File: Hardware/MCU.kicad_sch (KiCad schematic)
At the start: 18 parts, among them SW1 SW_Push, SW2 SW_SPDT, U1 STM32F405RGTx, Y1 Crystal

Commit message: Edited schematics
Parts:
- added C15: 100nF, symbol Device:C
- added J3: Conn_01x04_Pin, symbol Connector:Conn_01x04_Pin
- added R4, R5: 0, symbol Device:R
- added R6, R7: 10k, symbol Device:R
- C11: value 10uF -> 100nF
- C12, C13: value C -> 2.2uF
- R1: value R -> 10k
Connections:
- net +3.3V: now also J3.1 (Pin_1), R4.2, R5.2
- net GND: now also C15.2, J3.2 (Pin_2), R6.2
- net Baro_SCK: now reaches U1.21 (PA5)
- net Baro_MISO: now reaches U1.22 (PA6)
- net Baro_MOSI: now reaches U1.23 (PA7)
- net Baro_SS: now reaches U1.24 (PC4)
- net V_sense: now reaches U1.27 (PB1)
- net V_sense: now also C15.1, R6.1, R7.2
- net Buzz: now reaches U1.29 (PB10)
- net ADXL_SS: now reaches U1.33 (PB12)
- net Acc_Gyro_CLK: now reaches U1.34 (PB13)
- net Acc_Gyro_MISO: now reaches U1.35 (PB14)
- net Acc_Gyro_MOSI: now reaches U1.36 (PB15)
- net ICM_SS: now reaches U1.37 (PC6)
- net SDIO_D0: now reaches U1.39 (PC8)
- net SDIO_D1: now reaches U1.40 (PC9)
- net Relay1: now reaches U1.41 (PA8)
- net Relay2: now reaches U1.42 (PA9)
- net Relay3: now reaches U1.43 (PA10)
- net USB_D-: now reaches U1.44 (PA11)
- net USB_D+: now reaches U1.45 (PA12)
- net SWDIO: now reaches U1.46 (PA13)
- net SWDIO: now also J3.3 (Pin_3)
- net SWCLK: now reaches U1.49 (PA14)
- net SWCLK: now also J3.4 (Pin_4)
- net SDIO_D2: now reaches U1.51 (PC10)
- net SDIO_D3: now reaches U1.52 (PC11)
- net SDIO_CLK: now reaches U1.53 (PC12)
- net SDIO_CMD: now reaches U1.54 (PD2)
- net RF_TX: now reaches U1.58 (PB6)
- net RF_RX: now reaches U1.59 (PB7)
- net GPS_SCL: now reaches U1.61 (PB8)
- net GPS_SCL: now also R4.1
- net GPS_SDA: now reaches U1.62 (PB9)
- net GPS_SDA: now also R5.1
- new net +BATT: R7.1
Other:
- note added: "2S Bat_V_max = 7.2"
- note added: "Programming pins"
- note added: "TODO: - Select footprint, components. - Add buzzer - Add RGB leds - Select crystal oscillator - Consider TC2030 connector"
- note added: "Voltage sensing"
- note removed: "MCU"
- company: (none) -> Burocket
- title: (none) -> MCU
- moved on the sheet: C11, C12, C13, R1, SW1, SW2, U1

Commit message: Selected components and added their properties, started the power schematics
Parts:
- removed C9: C, symbol Device:C
- added C16: 2.2uF, Capacitor_SMD:C_0402_1005Metric, symbol Device:C
- added C17: 100nF, Capacitor_SMD:C_0402_1005Metric, symbol Device:C
- added C18: 20pF, Capacitor_SMD:C_0603_1608Metric, symbol Device:C
- added D1: Blue_LED, Capacitor_SMD:C_0603_1608Metric, symbol Device:LED
- added D2: Red LED, Capacitor_SMD:C_0603_1608Metric, symbol Device:LED
- added FB1: FerriteBead, symbol Device:FerriteBead
- added R10, R9: 1k, Resistor_SMD:R_0402_1005Metric, symbol Device:R
- C1, C11, C15, C2, C3, C4, C5, C6, C7: footprint (none) -> Capacitor_SMD:C_0402_1005Metric; Distributer Link (none) -> https://www.ozdisan.com/p/smt-smd-ve-mlcc-kapasitorler-184/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; Part Number (none) -> GRT155R71E104KE01D
- C10: value C -> 20pF; footprint (none) -> Capacitor_SMD:C_0603_1608Metric; Distributer Link (none) -> https://www.ozdisan.com/p/smt-smd-ve-mlcc-kapasitorler-184/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; Part Number (none) -> CC0603JRNPO9BN200
- C12, C13: footprint (none) -> Capacitor_SMD:C_0402_1005Metric; Distributer Link (none) -> http://ozdisan.com/p/smt-smd-ve-mlcc-kapasitorler-184/murat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; Part Number (none) -> GRT155C81A225ME13D
- C8: footprint (none) -> Capacitor_SMD:C_0805_2012Metric; Distributer Link (none) -> https://www.ozdisan.com/p/tantal-kapasitorler-178/kyocera-a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; Part Number (none) -> TAJR106K006RNJ
- J3: footprint (none) -> Connector_PinHeader_2.54mm:PinHeader_1x04_P2.54mm_Vertical; now left out of the parts list
- R1, R6, R7: footprint (none) -> Resistor_SMD:R_0603_1608Metric; Distributer Link (none) -> https://www.ozdisan.com/p/smt-smd-ve-cip-direncler-194/roya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; Part Number (none) -> CQ03SAJ0103T5E
- SW1: footprint (none) -> Button_Switch_SMD:SW_SPST_PTS810; Distributer Link (none) -> https://www.ozdisan.com/p/tact-sivicler-485/littelfuse-ck-p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; Part Number (none) -> PTS815SJK250SMTRLFS
- SW2: footprint (none) -> Button_Switch_SMD:SW_SPDT_CK_JS102011SAQN; Distributer Link (none) -> https://www.ozdisan.com/p/surgulu-sivicler-495/kls-electron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; Part Number (none) -> L-KLS7-MSK-12C03
- Y1: value Crystal -> 25Mhz; footprint (none) -> footprints:Custom_Oscillator; Distributer Link (none) -> https://www.ozdisan.com/p/osilatorler-510/raltron-com1305-2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; Part Number (none) -> COM1305-25.000-EXT-T-TR
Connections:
- net +3.3V: now also C16.1, FB1.2; no longer C7.1
- net +BATT: now also R6.1; no longer R7.1
- net GND: now also R7.2, C16.2, C17.2, C18.2, D1.1 (K), D2.1 (K); no longer R6.2
- net NRST: now also C17.1
- net OSC_IN: now also C18.1
- net Relay1: now also U1.14 (PA0); no longer U1.41 (PA8)
- net Relay2: now also U1.15 (PA1); no longer U1.42 (PA9)
- net Relay3: now also U1.16 (PA2); no longer U1.43 (PA10)
- net V_sense: now also R6.2, R7.1; no longer R6.1, R7.2
- net ADC3: now reaches U1.10 (PC2)
- net ADC4: now reaches U1.11 (PC3)
- net Relay4: now reaches U1.17 (PA3)
- net Red_LED: now reaches U1.2 (PC13)
- net Red_LED: now also R10.1
- net Blue_LED: now reaches U1.3 (PC14)
- net Blue_LED: now also R9.1
- net ADC1: now reaches U1.8 (PC0)
- net ADC2: now reaches U1.9 (PC1)
- new net: C7.1, FB1.1
- new net: D2.2 (A), R9.2
- new net: D1.2 (A), R10.2
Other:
- note added: "Analog decoupling"
- note added: "C1 = C2 = 2*(Cl-Cs) C1 = C2 = 2*(15-5)"
- note removed: "C1 = C2 = 2*(Cl-Cs)"
- moved on the sheet: C10, J3, R1, SW1, SW2, Y1

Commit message: Added a simulations file, added App Notes file, Finalized SD-card design type shit
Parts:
- removed J3: Conn_01x04_Pin, Connector_PinHeader_2.54mm:PinHeader_1x04_P2.54mm_Vertical, symbol Connector:Conn_01x04_Pin
- added J5: Conn_01x05_Pin, symbol Connector:Conn_01x05_Pin
- added R26: 0, Resistor_SMD:R_0402_1005Metric, symbol Device:R
- R1, R6: Distributer Link https://www.ozdisan.com/p/smt-smd-ve-cip-direncler-194/roya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 -> https://www.ozdisan.com/p/smt-smd-ve-cip-direncler-194/pana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; Part Number CQ03SAJ0103T5E -> ERJ3EKF1002V
- R4, R5: value 0 -> 2.2k
- R7: value 10k -> 5.1k; footprint Resistor_SMD:R_0603_1608Metric -> Resistor_SMD:R_0402_1005Metric; Distributer Link https://www.ozdisan.com/p/smt-smd-ve-cip-direncler-194/roya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 -> https://www.ozdisan.com/p/smt-smd-ve-cip-direncler-194/pana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; Part Number CQ03SAJ0103T5E -> ERJ2RKF5101X
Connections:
- net +3.3V: now also J5.1 (Pin_1)
- net Buzz: now also U1.38 (PC7); no longer U1.29 (PB10)
- net GND: now also J5.2 (Pin_2)
- net Relay1: now also U1.27 (PB1); no longer U1.14 (PA0)
- net Relay2: now also U1.28 (PB2); no longer U1.15 (PA1)
- net Relay3: now also U1.29 (PB10); no longer U1.16 (PA2)
- net Relay4: now also U1.30 (PB11); no longer U1.17 (PA3)
- net SWCLK: now also J5.4 (Pin_4)
- net SWDIO: now also J5.3 (Pin_3)
- net V_sense: now also U1.26 (PB0), R26.2; no longer R6.2, R7.1, U1.27 (PB1)
- net SDIO_CDS: now reaches U1.50 (PA15)
- net SWO: now reaches U1.55 (PB3)
- net SWO: now also J5.5 (Pin_5)
- new net: R26.1, R6.2, R7.1
- no-connect marks 0 -> 12
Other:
- note added: "2S Bat_V_max = 8.4"
- note added: "5.1k/(5.1k + 10k)*8.4V=2.83V Max voltage"
- note added: "MCU"
- note added: "Programming & Debugging pins"
- note removed: "2S Bat_V_max = 7.2"
- note removed: "Programming pins"
- note removed: "TODO: - Select footprint, components. - Add buzzer - Add RGB leds - Select crystal oscillator - Consider TC2030 connector"
- moved on the sheet: C10, C11, C12, C13, C15, C17, C18, D1, D2, R1, R10, R4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

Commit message: +1000 Aura
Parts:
- added BZ1: Buzzer, symbol Device:Buzzer
- added C33, C34: C, symbol Device:C
- added D5, D6: D, symbol Device:D
- added Q1: NPN, symbol Simulation_SPICE:NPN
- added R27, R28: R, symbol Device:R
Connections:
- net GND: now also C33.2, C34.2, Q1.3 (E)
- net BUZZER: now reaches U1.57 (PB5)
- net BUZZER: now also R28.2
- new net: BZ1.2 (-), Q1.1 (C)
- new net: Q1.2 (B), R28.1
- new net: D5.1 (K), R27.1
- new net: BZ1.1 (+), C34.1, R27.2
- new net: D5.2 (A), D6.1 (K)
- new net +5V: C33.1, D6.2 (A)
- no-connect marks 12 -> 11
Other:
- note added: "Buzzer"
- note added: "To be designed"
- moved on the sheet: C1, C12, C13, C16, C2, C3, C4, C5, C6, C7, C8, FB1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

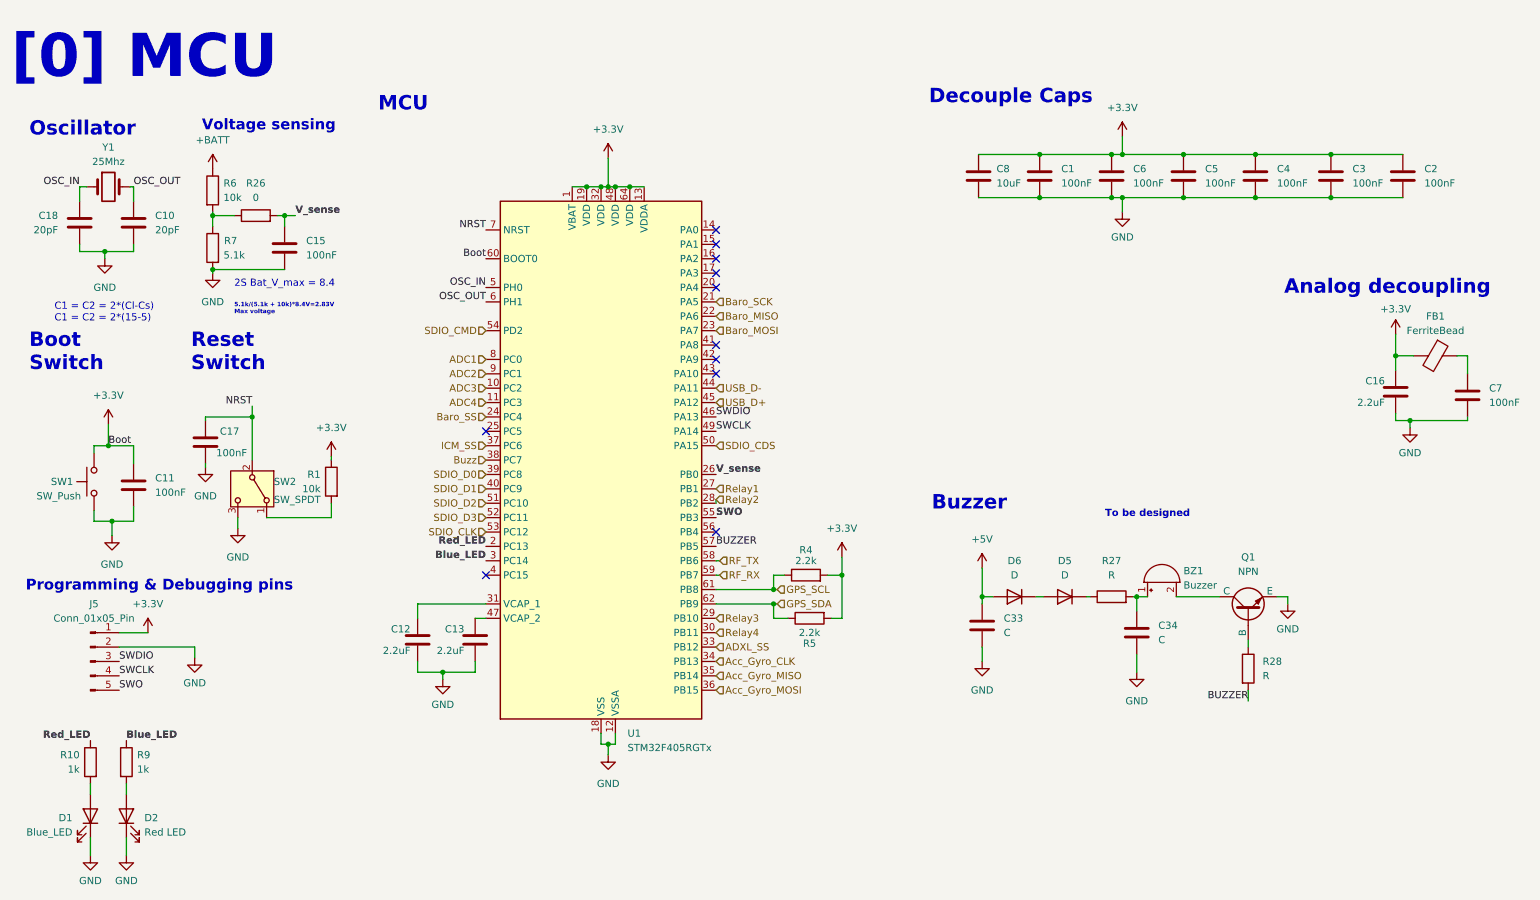
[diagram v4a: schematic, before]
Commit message: Only SSR and ferrite bead selection is left
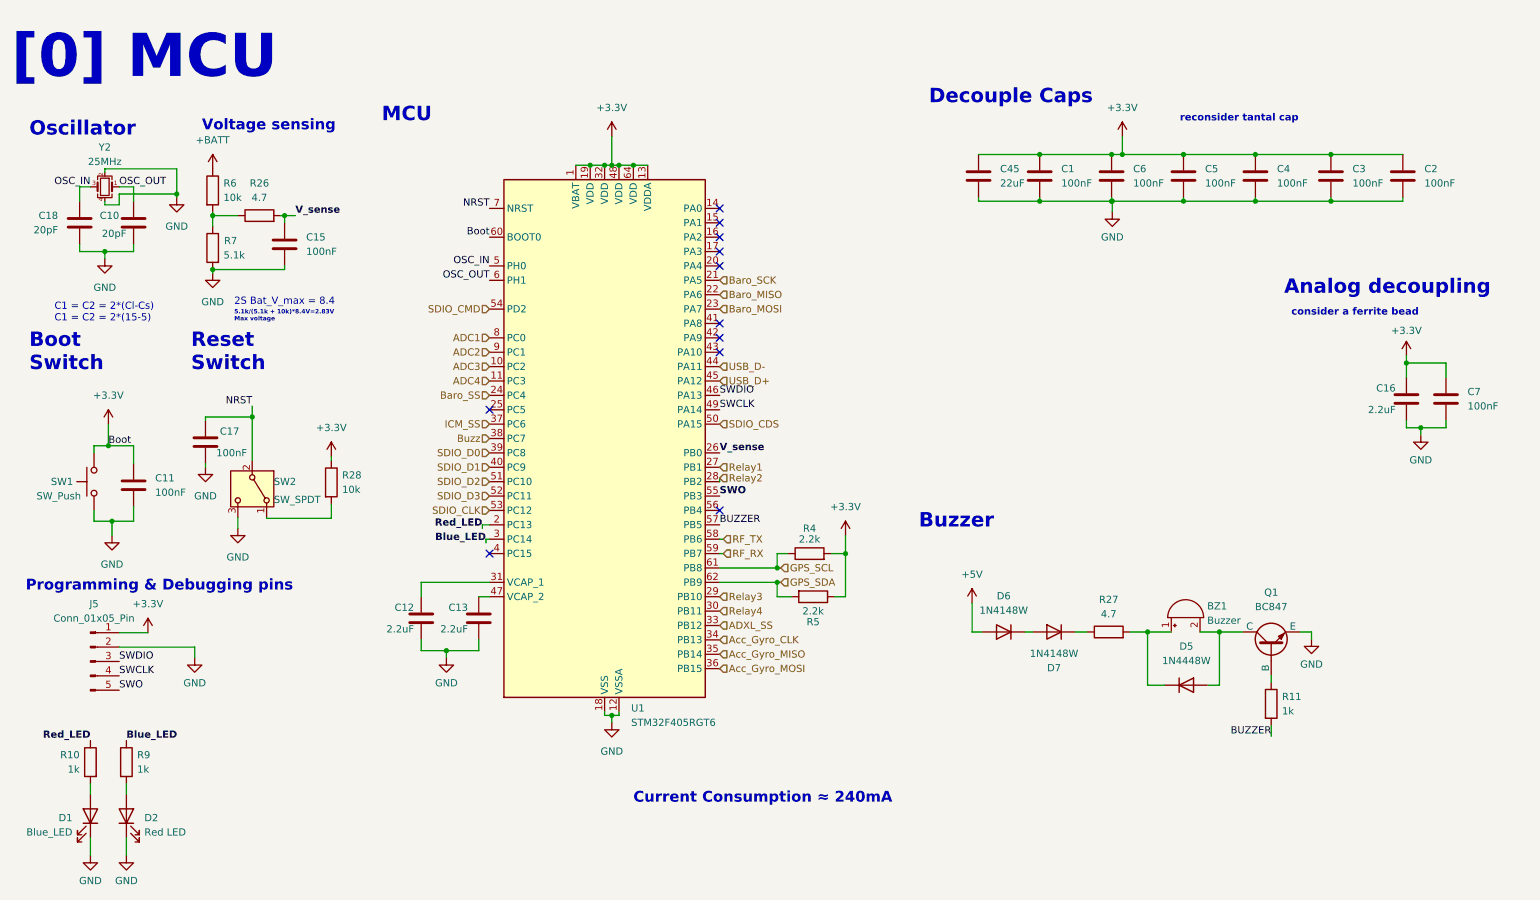
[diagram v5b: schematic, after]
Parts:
- removed C33, C34: C, symbol Device:C
- removed C8: 10uF, Capacitor_SMD:C_0805_2012Metric, symbol Device:C
- removed FB1: FerriteBead, symbol Device:FerriteBead
- removed R1: 10k, Resistor_SMD:R_0603_1608Metric, symbol Device:R
- removed Y1: 25Mhz, footprints:Custom_Oscillator, symbol Device:Crystal
- added C45: 22uF, Capacitor_SMD:C_0805_2012Metric, symbol Device:C
- added D7: 1N4148W, Diode_SMD:D_SOD-123, symbol Device:D
- added R11: 1k, Resistor_SMD:R_0402_1005Metric, symbol Device:R
- added Y2: 25MHz, Crystal:Crystal_SMD_3225-4Pin_3.2x2.5mm, symbol Device:Crystal_GND24_Small
- BZ1: footprint (none) -> footprints:Buzzer_typeshit; Distributer Link (none) -> https://www.ozdisan.com/p/buzzerlar-430/kls-electronic-l-kl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; Part Number (none) -> L-KLS3-SMT-3020-3V
- D5: value D -> 1N4448W; footprint (none) -> Diode_SMD:Nexperia_CFP3_SOD-123W; Distributer Link (none) -> https://www.ozdisan.com/p/dogrultucu-diyotlar-389/panjit-1n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; Part Number (none) -> 1N4448W_R1_00001
- D6: value D -> 1N4148W; footprint (none) -> Diode_SMD:D_SOD-123; Distributer Link (none) -> https://www.ozdisan.com/p/dogrultucu-diyotlar-389/panjit-1n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; Part Number (none) -> 1N4148W-AU_R1_000A1
- J5: footprint (none) -> Connector_PinHeader_2.54mm:PinHeader_1x05_P2.54mm_Vertical; now left out of the parts list
- Q1: value NPN -> BC847; footprint (none) -> Package_TO_SOT_SMD:SOT-323_SC-70; Distributer Link (none) -> https://www.ozdisan.com/p/discrete-transistorler-442/onsem-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; Part Number (none) -> BC847CWT1G
- R26: value 0 -> 4.7; Distributer Link (none) -> https://www.ozdisan.com/p/smt-smd-ve-cip-direncler-194/roya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; Part Number (none) -> CQ02WGJ047JTCE
- R27: value R -> 4.7; footprint (none) -> Resistor_SMD:R_0402_1005Metric; Distributer Link (none) -> https://www.ozdisan.com/p/smt-smd-ve-cip-direncler-194/roya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; Part Number (none) -> CQ02WGJ047JTCE
- R28: value R -> 10k; footprint (none) -> Resistor_SMD:R_0402_1005Metric; Distributer Link (none) -> https://www.ozdisan.com/p/smt-smd-ve-cip-direncler-194/roya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; Part Number (none) -> CQ02WGF1002TCE
- R4, R5: footprint (none) -> Resistor_SMD:R_0402_1005Metric; Distributer Link (none) -> https://www.ozdisan.com/p/smt-smd-ve-cip-direncler-194/roya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; Part Number (none) -> HP02WAF2201TCE
- R6: footprint Resistor_SMD:R_0603_1608Metric -> Resistor_SMD:R_0402_1005Metric; Distributer Link https://www.ozdisan.com/p/smt-smd-ve-cip-direncler-194/pana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 -> https://www.ozdisan.com/p/smt-smd-ve-cip-direncler-194/roya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; Part Number ERJ3EKF1002V -> CQ02WGF1002TCE
- U1: value STM32F405RGTx -> STM32F405RGT6
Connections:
- net +3.3V: now also C7.1, R28.1, R5.1, C45.1; no longer R5.2
- net BUZZER: now also R11.2; no longer R28.2
- net GND: now also C45.2, Y2.2, Y2.4
- net GPS_SDA: now also R5.2; no longer R5.1
- net OSC_IN: now also Y2.3
- net OSC_OUT: now also Y2.1
- net at SW2.1 (A): now also R28.2
- net at BZ1.2 (-), Q1.1 (C): now also D5.2 (A)
- net at Q1.2 (B): now also R11.1; no longer R28.1
- net at D5.1 (K): now also BZ1.1 (+), R27.2; no longer R27.1
- net at D6.1 (K): now also D7.2 (A); no longer D5.2 (A)
- new net: D7.1 (K), R27.1
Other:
- note added: "Current Consumption ≈ 240mA"
- note added: "consider a ferrite bead"
- note added: "reconsider tantal cap"
- note removed: "To be designed"
- moved on the sheet: BZ1, C12, C13, C15, C16, C7, D6, Q1, R26, R4, U1

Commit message: Ne yazacagimi bilemedim
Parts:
- added FB1: FerriteBead, symbol Device:FerriteBead
- added R53: 10k, Resistor_SMD:R_0402_1005Metric, symbol Device:R
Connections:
- net +3.3V: now also FB1.2, R53.1; no longer C11.1, C7.1, SW1.2, U1.60 (BOOT0)
- net NRST: no longer C17.1, SW2.2 (B)
- net USB_D+: now also U1.44 (PA11); no longer U1.45 (PA12)
- net USB_D-: now also U1.45 (PA12); no longer U1.44 (PA11)
- net Baro_MISO renamed BARO_MISO
- net Baro_MOSI renamed BARO_MOSI
- net Baro_SCK renamed BARO_SCK
- net Baro_SS renamed BARO_SS
- net Buzz: no longer names the net of U1.38 (PC7)
- new net: C11.1, R53.2, SW1.2
- new net: C7.1, FB1.1
- new net Boot: C17.1, SW2.2 (B), U1.60 (BOOT0)
- no-connect marks 11 -> 12
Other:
- note added: "MAX Current Consumption ≈ 240mA"
- note removed: "Current Consumption ≈ 240mA"
- moved on the sheet: C7, R4, R5

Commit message: Commit bulamadim :)
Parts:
- removed C15: 100nF, Capacitor_SMD:C_0402_1005Metric, symbol Device:C
- removed R4, R5: 2.2k, Resistor_SMD:R_0402_1005Metric, symbol Device:R
- R26: value 4.7 -> 10k; Distributer Link https://www.ozdisan.com/p/smt-smd-ve-cip-direncler-194/royalohm-cq02wgj047jtce-587859 -> https://www.ozdisan.com/p/smt-smd-ve-cip-direncler-194/royalohm-cq02wgf1002tce-587902; Part Number CQ02WGJ047JTCE -> CQ02WGF1002TCE
- R7: value 5.1k -> 10k; Distributer Link https://www.ozdisan.com/p/smt-smd-ve-cip-direncler-194/pana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 -> https://www.ozdisan.com/p/smt-smd-ve-cip-direncler-194/roya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; Part Number ERJ2RKF5101X -> CQ02WGF1002TCE
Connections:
- net GPS_SDA is gone; now on net Sense_SDA: U1.62 (PB9)
- net +3.3V: now also R26.2, R7.2
- net BUZZER: now also U1.26 (PB0); no longer U1.57 (PB5)
- net GND: no longer R7.2
- net RF_RX: now also U1.17 (PA3); no longer U1.59 (PB7)
- net RF_TX: now also U1.16 (PA2); no longer U1.58 (PB6)
- net RF_M0: now reaches U1.14 (PA0)
- net RF_M1: now reaches U1.15 (PA1)
- net RF_AUX: now reaches U1.20 (PA4)
- net Flash_SS: now reaches U1.25 (PC5)
- net Sense_alert: now reaches U1.42 (PA9)
- net Sense_alert: now also R26.1
- net GPS_RESET: now reaches U1.56 (PB4)
- net +BATT renamed Sense_SDA
- net GPS_SCL renamed Sense_SCL
- net Sense_SCL: now also R7.1
- removed net V_sense: R26.2, U1.26 (PB0)
- new net GPS_EXTI: U1.57 (PB5)
- new net GPS_RX: U1.59 (PB7)
- new net GPS_TX: U1.58 (PB6)
- now unconnected: R6.2
- no-connect marks 12 -> 4
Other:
- note removed: "2S Bat_V_max = 8.4"
- note removed: "5.1k/(5.1k + 10k)*8.4V=2.83V Max voltage"
- note removed: "Voltage sensing"
- moved on the sheet: BZ1, C16, C7, D1, D2, D5, D6, D7, FB1, J5, Q1, R10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
